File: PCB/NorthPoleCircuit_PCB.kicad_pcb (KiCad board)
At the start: 4 copper layers, 155 x 110 mm, 161 parts, among them J1 USB_C_Receptacle_USB2.0_16P, J3 PROG, J4 PROG, SW1 TS-1088-AR02016, SW2 TS-1088-AR02016, SW3 TS-1187A-C-E-B, U1 DRV5032FADMRR, U10 DRV8837, U11 DRV8837, U2 CH592X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

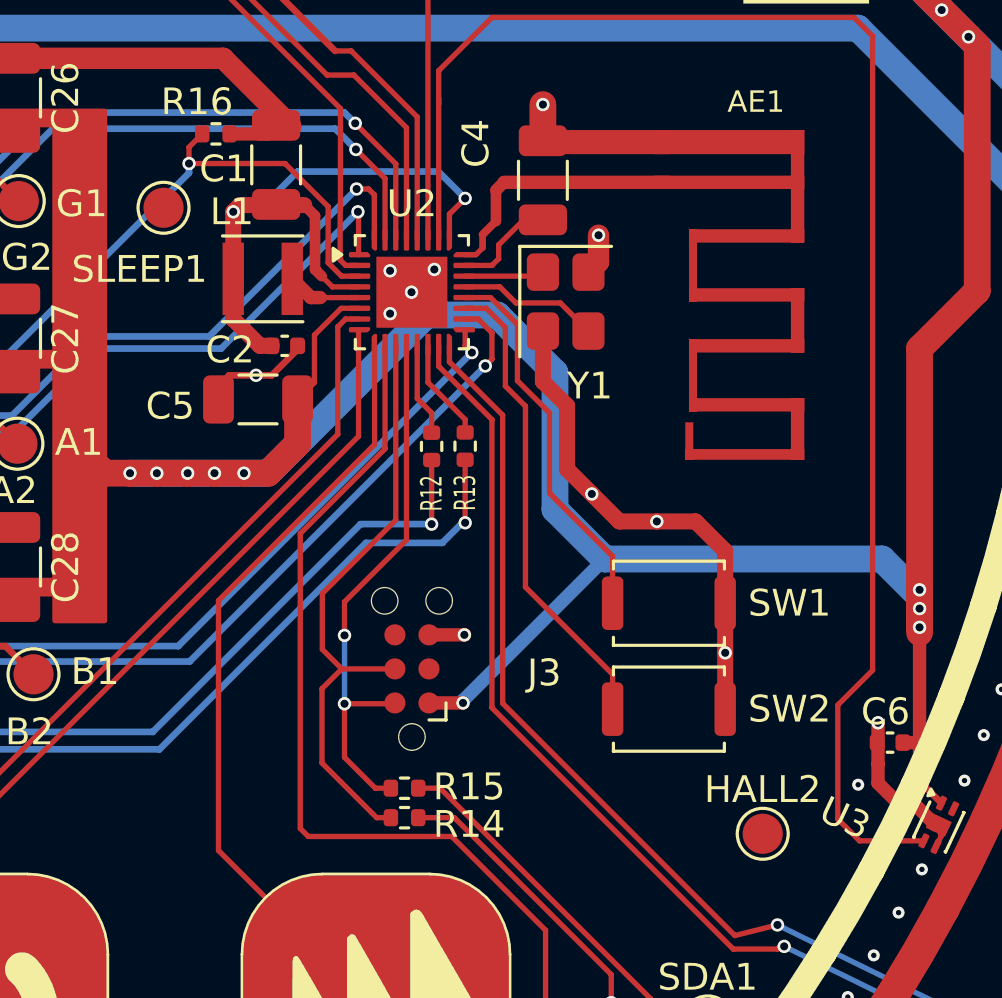
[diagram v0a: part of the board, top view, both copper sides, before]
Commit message: First tests on real PCB. PCB is alive. FW comfirms most of the functionality including BLE. Hall sensor has footprint bug. IP5209 chip still not charging the battery. LED is producing only WHITE.
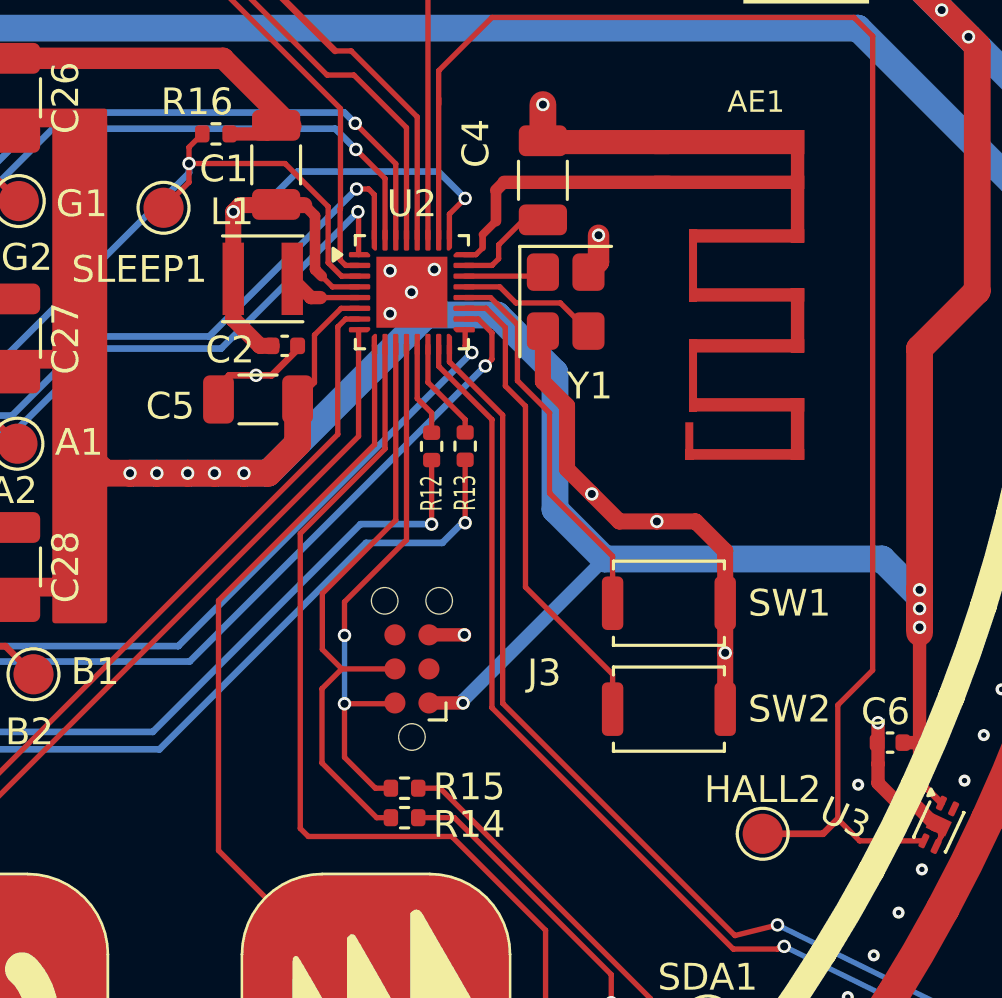
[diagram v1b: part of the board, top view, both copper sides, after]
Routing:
- net /HALL2: track 57.1 -> 60.1 mm
- net /SLEEP: track 46.3 -> 48.4 mm
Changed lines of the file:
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@@
 	)
 	(segment
+		(start 165.2 84.7)
+		(end 165.2 85.4)
+		(width 0.2)
+		(layer "F.Cu")
+		(net "/SLEEP")
+	)
+	(segment
 		(start 165.2 84.09)
 		(end 165.695 83.595)
@@
 	)
 	(segment
+		(start 165.2 85.4)
+		(end 164.25 86.35)
+		(width 0.2)
+		(layer "F.Cu")
+		(net "/SLEEP")
+	)
+	(segment
 		(start 168.784386 84.7)
 		(end 165.2 84.7)
@@
 	)
 	(segment
+		(start 186.6 109.7)
+		(end 188.85 109.7)
+		(width 0.25)
+		(layer "F.Cu")
+		(net "/HALL2")
+	)
+	(segment
 		(start 190.7 79.95)
 		(end 190.7 103.6)
@@
 		(layer "F.Cu")
 		(net "/HALL2")
+	)
+	(segment
+		(start 188.85 109.7)
+		(end 189.4 109.15)
+		(width 0.25)
+		(layer "F.Cu")
+		(net "/HALL2")
